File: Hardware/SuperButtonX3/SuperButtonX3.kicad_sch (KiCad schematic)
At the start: 21 parts, among them J101 USBC, J103 EXT_LED, SW101 Switch, SW201 PROG, U101 CH552G

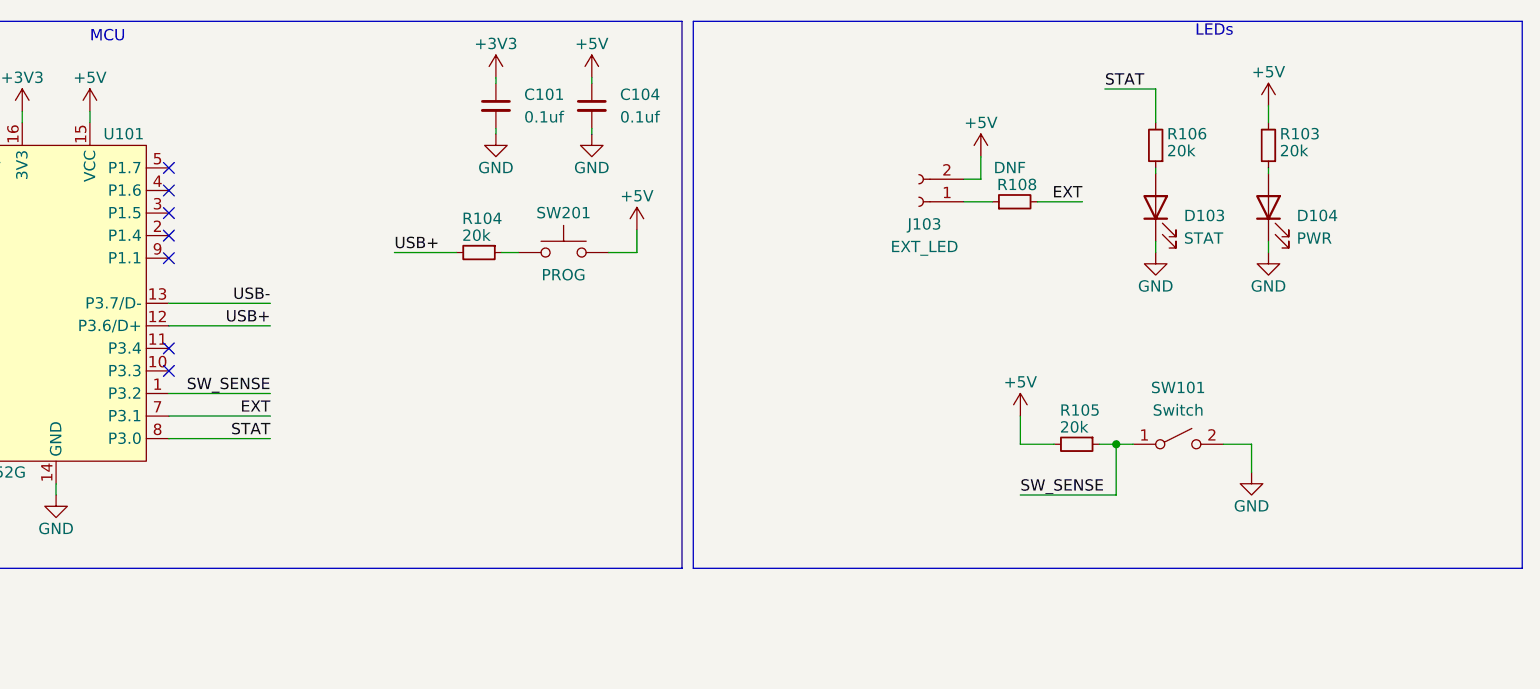
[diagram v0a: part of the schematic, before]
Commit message: increased width of board, moved a couple of the components around to help better fit the wiring for the two new buttons, not finished yet.
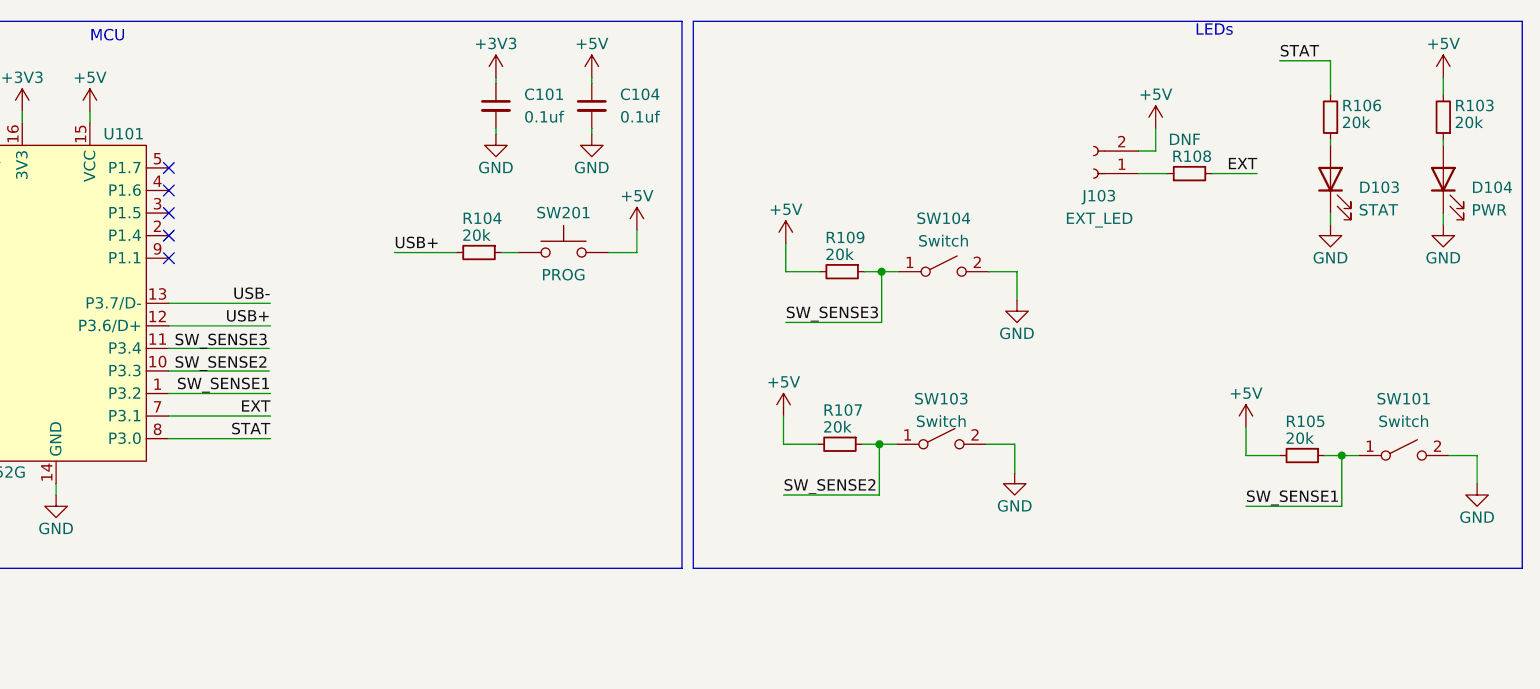
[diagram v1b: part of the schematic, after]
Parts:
- added R107, R109: 20k, Resistor_SMD:R_0805_2012Metric, symbol Device:R_Small
- added SW103, SW104: Switch, Switch_Keyboard_Cherry_MX:SW_Cherry_MX_PCB, symbol Switch:SW_SPST
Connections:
- net +5V: now also R107.2, R109.2
- net GND: now also SW103.2 (B), SW104.2 (B)
- net SW_SENSE renamed SW_SENSE1
- new net SW_SENSE2: R107.1, SW103.1 (A)
- new net SW_SENSE3: R109.1, SW104.1 (A)
- no-connect marks 9 -> 7
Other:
- moved on the sheet: D103, D104, J103, R103, R105, R106, R108, SW101
